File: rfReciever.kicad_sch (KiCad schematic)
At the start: 38 parts, among them J1 MOLEX 1054440001, SW1 RF_RESET, SW2 RF_SLEEP, U1 CP2102N-A02-GQFN24, U2 USBLC6-2SC6, X1 DigiXBeeRX900Micro

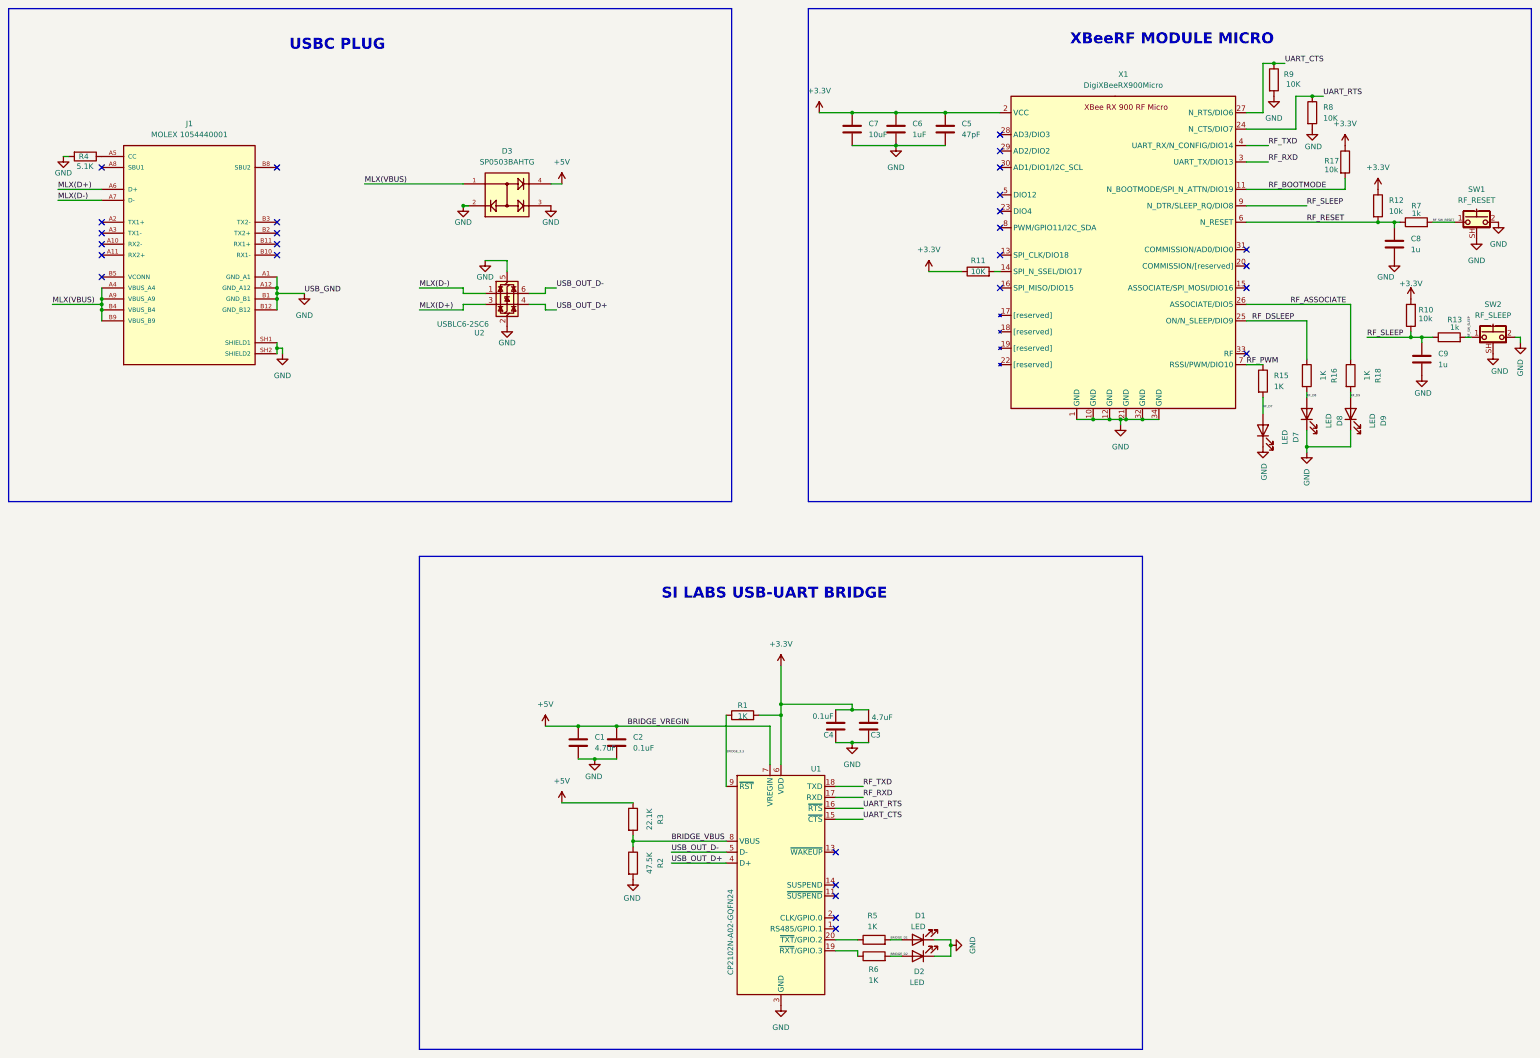
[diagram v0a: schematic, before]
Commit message: updated schematic with new bridge and LDO (label "VCCIO" (at 228.6 199.39 0) (fields_autoplaced yes)   (effects (font (size 1.27 1.27)) (justify left bottom)) (uuid "1f50f597-85ab-42bc-9a9f-0ec370d6b6a6") )
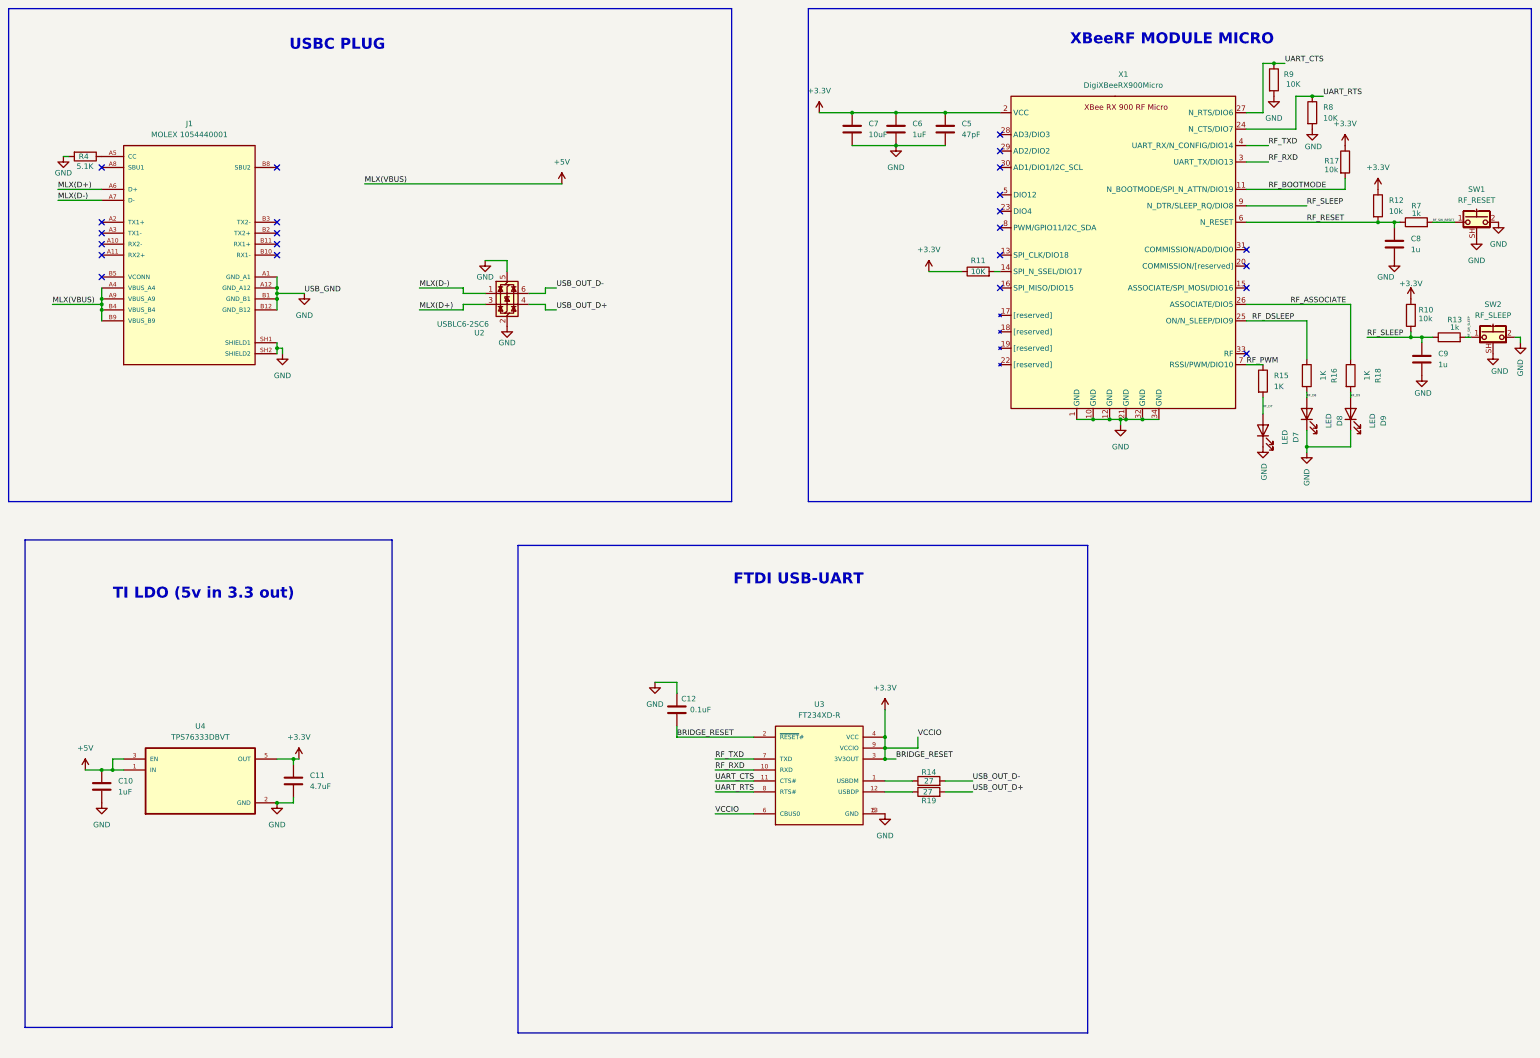
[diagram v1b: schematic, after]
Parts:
- removed C1, C3: 4.7uF, Capacitor_SMD:C_0805_2012Metric, symbol Device:C
- removed C2, C4: 0.1uF, Capacitor_SMD:C_0805_2012Metric, symbol Device:C
- removed D1, D2: LED, LED_SMD:LED_0805_2012Metric, symbol Device:LED
- removed D3: SP0503BAHTG, rfReciever-Footprints:SOT143, symbol 5vESD:SP0503BAHTG
- removed R1, R5, R6: 1K, Resistor_SMD:R_0805_2012Metric, symbol Device:R
- removed R2: 47.5K, Resistor_SMD:R_0805_2012Metric, symbol Device:R
- removed R3: 22.1K, Resistor_SMD:R_0805_2012Metric, symbol Device:R
- removed U1: CP2102N-A02-GQFN24, rfReciever-Footprints:QFN50P500X500X80-29N, symbol Interface_USB:CP2102N-Axx-xQFN20
- added C10: 1uF, Capacitor_SMD:C_0805_2012Metric, symbol Device:C
- added C11: 4.7uF, Capacitor_SMD:C_0805_2012Metric, symbol Device:C
- added C12: 0.1uF, Capacitor_SMD:C_0805_2012Metric, symbol Device:C
- added R14, R19: 27, Resistor_SMD:R_0805_2012Metric, symbol Device:R
- added U3: FT234XD-R, FT234XD-R:SON45P300X300X80-13N, symbol FTDIBridge:FT234XD-R
- added U4: TPS76333DBVT, TPS76333DBVT:SOT95P280X145-5N, symbol ExternalLDO:TPS76333DBVT
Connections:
- net MLX(VBUS) is gone; now on net +5V: J1.A4 (VBUS_A4), J1.A9 (VBUS_A9), J1.B4 (VBUS_B4), J1.B9 (VBUS_B9)
- net +3.3V: now also C11.1, C12.2, U3.2 (~{RESET}#), U3.3 (3V3OUT), U3.4 (VCC), U3.6 (CBUS0), U3.9 (VCCIO), U4.5 (OUT)
- net +5V: now also C10.1, U4.1 (IN), U4.3 (EN)
- net GND: now also C10.2, C11.2, C12.1, U3.13 (GND), U3.5 (GND), U4.2 (GND)
- net RF_RXD: now also U3.10 (RXD)
- net RF_TXD: now also U3.7 (TXD)
- net UART_CTS: now also U3.11 (CTS#)
- net UART_RTS: now also U3.8 (RTS#)
- net USB_OUT_D+: now also R19.2
- net USB_OUT_D-: now also R14.2
- new net: R19.1, U3.12 (USBDP)
- new net: R14.1, U3.1 (USBDM)
- no-connect marks 28 -> 23
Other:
- note added: "FTDI USB-UART"
- note added: "TI LDO (5v in 3.3 out)"
- note removed: "SI LABS USB-UART BRIDGE"

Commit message: reworked schematic v1 matthew review
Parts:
- removed C12: 0.1uF, Capacitor_SMD:C_0805_2012Metric, symbol Device:C
- added C1: 10nF, symbol Device:C
- added R1: 10K, Resistor_SMD:R_0805_2012Metric, symbol Device:R
- U3: footprint FT234XD-R:SON45P300X300X80-13N -> rfReciever-Footprints:SON45P300X300X80-13N
- U4: footprint TPS76333DBVT:SOT95P280X145-5N -> rfReciever-Footprints:SOT95P280X145-5N
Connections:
- net +3.3V: now also R1.2; no longer U3.2 (~{RESET}#), U3.6 (CBUS0)
- net GND: now also C1.2
- new net: C1.1, R1.1, U3.2 (~{RESET}#)
- new net VCCIO: U3.6 (CBUS0)
